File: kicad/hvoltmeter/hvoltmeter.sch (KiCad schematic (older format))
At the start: 34 parts, among them J1 USB_B_Micro-Connector, J2 SWC, J3 SWD, J4 Conn, J5 Conn, J6 Conn, SW1 SW_DPDT_x2, U1 LTC4054ES5-4.2, U2 AD8541, U3 MCP1700

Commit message: удалено:       STM32Cube/HV/.cproject 	удалено:       STM32Cube/HV/.mxproject 	удалено:       STM32Cube/HV/.project 	удалено:       STM32Cube/HV/.settings/language.settings.xml 	удалено:       STM32Cube/HV/.settings/stm32cubeide.project.prefs 	удалено:       STM32Cube/HV/Core/Inc/main.h 	удалено:       STM32Cube/HV/Core/Inc/stm32g0xx_hal_conf.h 	удалено:       STM32Cube/HV/Core/Inc/stm32g0xx_it.h 	удалено:       STM32Cube/HV/Core/Src/main.c 	удалено:       STM32Cube/HV/Core/Src/stm32g0xx_hal_msp.c 	удалено:       STM32Cube/HV/Core/Src/stm32g0xx_it.c 	удалено:       STM32Cube/HV/Core/Src/syscalls.c 	удалено:       STM32Cube/HV/Core/Src/sysmem.c 	удалено:       STM32Cube/HV/Core/Src/system_stm32g0xx.c 	удалено:       STM32Cube/HV/Core/Startup/startup_stm32g031f8px.s 	удалено:       STM32Cube/HV/Drivers/CMSIS/Device/ST/STM32G0xx/Include/stm32g031xx.h 	удалено:       STM32Cube/HV/Drivers/CMSIS/Device/ST/STM32G0xx/Include/stm32g0xx.h 	удалено:       STM32Cube/HV/Drivers/CMSIS/Device/ST/STM32G0xx/Include/system_stm32g0xx.h 	удалено:       STM32Cube/HV/Drivers/CMSIS/Include/cmsis_armcc.h 	удалено:       STM32Cube/HV/Drivers/CMSIS/Include/cmsis_armclang.h 	удалено:       STM32Cube/HV/Drivers/CMSIS/Include/cmsis_armclang_ltm.h 	удалено:       STM32Cube/HV/Drivers/CMSIS/Include/cmsis_compiler.h 	удалено:       STM32Cube/HV/Drivers/CMSIS/Include/cmsis_gcc.h 	удалено:       STM32Cube/HV/Drivers/CMSIS/Include/cmsis_iccarm.h 	удалено:       STM32Cube/HV/Drivers/CMSIS/Include/cmsis_version.h 	удалено:       STM32Cube/HV/Drivers/CMSIS/Include/core_armv81mml.h 	удалено:       STM32Cube/HV/Drivers/CMSIS/Include/core_armv8mbl.h 	удалено:       STM32Cube/HV/Drivers/CMSIS/Include/core_armv8mml.h 	удалено:       STM32Cube/HV/Drivers/CMSIS/Include/core_cm0.h 	удалено:       STM32Cube/HV/Drivers/CMSIS/Include/core_cm0plus.h 	удалено:       STM32Cube/HV/Drivers/CMSIS/Include/core_cm1.h 	удалено:       STM32Cube/HV/Drivers/CMSIS/Include/core_cm23.h 	удалено:       STM32Cube/HV/Drivers/CMSIS/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
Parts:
- D2: symbol My_Library:STM32G031F8-My_Library -> hvoltmeter-rescue:STM32G031F8-My_Library-My_Library
- D3: symbol My_Library:OLED049 -> hvoltmeter-rescue:OLED049-My_Library
- J1: symbol My_Library:USB_B_Micro-Connector -> hvoltmeter-rescue:USB_B_Micro-Connector-My_Library
- J2, J3, J4, J5, J6: symbol My_Library:Conn -> hvoltmeter-rescue:Conn-My_Library
- R6: value 10G -> 5G
- R8: value 4.7k -> 10k
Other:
- moved on the sheet: R8
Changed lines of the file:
@@
 $EndComp
 $Comp
-L My_Library:USB_B_Micro-Connector J1
+L hvoltmeter-rescue:USB_B_Micro-Connector-My_Library J1
 U 1 1 632D2EFA
 P 2650 3000
@@
 $EndComp
 $Comp
-L My_Library:STM32G031F8-My_Library D2
+L hvoltmeter-rescue:STM32G031F8-My_Library-My_Library D2
 U 1 1 632D3B69
 P 2900 4550
@@
 $EndComp
 $Comp
-L My_Library:Conn J4
+L hvoltmeter-rescue:Conn-My_Library J4
 U 1 1 632DFC6A
 P 4450 3200
@@
 Connection ~ 3900 3700
 $Comp
-L My_Library:Conn J5
+L hvoltmeter-rescue:Conn-My_Library J5
 U 1 1 632FDD5C
 P 4450 3600
@@
 U 1 1 63336864
 P 4750 4850
-F 0 "R6" H 4820 4896 50  0000 L CNN
-F 1 "10G" H 4820 4805 50  0000 L CNN
+F 0 "R6" H 4550 5100 50  0000 L CNN
+F 1 "5G" H 4550 5000 50  0000 L CNN
 F 2 "Resistor_SMD:R_2512_6332Metric" V 4680 4850 50  0001 C CNN
 F 3 "~" H 4750 4850 50  0001 C CNN
@@
 $EndComp
 $Comp
-L My_Library:Conn J6
+L hvoltmeter-rescue:Conn-My_Library J6
 U 1 1 6334DD34
 P 4750 4600
@@
 NoConn ~ 3350 4800
 $Comp
-L My_Library:Conn J3
+L hvoltmeter-rescue:Conn-My_Library J3
 U 1 1 633707DA
 P 3450 4300
@@
 Connection ~ 5600 3000
 $Comp
-L My_Library:Conn J2
+L hvoltmeter-rescue:Conn-My_Library J2
 U 1 1 6336FFB2
 P 3450 4200
@@
 $EndComp
 $Comp
-L My_Library:OLED049 D3
+L hvoltmeter-rescue:OLED049-My_Library D3
 U 1 1 6342BAD8
 P 5650 4300
@@
 L power:+2V8 #PWR016
 U 1 1 63592993
-P 5150 4300
-F 0 "#PWR016" H 5150 4150 50  0001 C CNN
-F 1 "+2V8" V 5165 4428 50  0000 L CNN
-F 2 "" H 5150 4300 50  0001 C CNN
-F 3 "" H 5150 4300 50  0001 C CNN
-	1    5150 4300
+P 5000 4300
+F 0 "#PWR016" H 5000 4150 50  0001 C CNN
+F 1 "+2V8" V 5015 4428 50  0000 L CNN
+F 2 "" H 5000 4300 50  0001 C CNN
+F 3 "" H 5000 4300 50  0001 C CNN
+	1    5000 4300
 	0    -1   -1   0
 $EndComp
@@
 L Device:R R8
 U 1 1 6359D97D
-P 5300 4700
-F 0 "R8" V 5300 4600 50  0000 L CNN
-F 1 "4.7k" V 5400 4450 50  0000 L CNN
-F 2 "Resistor_SMD:R_0402_1005Metric" V 5230 4700 50  0001 C CNN
-F 3 "~" H 5300 4700 50  0001 C CNN
-	1    5300 4700
-	0    1    1    0
-$EndComp
-Wire Wire Line
-	5450 4600 5150 4600
-Wire Wire Line
-	5150 4600 5150 4700
-Connection ~ 5150 4600
+P 5000 4450
+F 0 "R8" H 5100 4400 50  0000 L CNN
+F 1 "10k" H 5100 4500 50  0000 L CNN
+F 2 "Resistor_SMD:R_0402_1005Metric" V 4930 4450 50  0001 C CNN
+F 3 "~" H 5000 4450 50  0001 C CNN
+	1    5000 4450
+	-1   0    0    1
+$EndComp
 Connection ~ 4600 5500
 Wire Wire Line
@@
 	4500 5550 4500 5300
 Wire Wire Line
-	5450 4300 5150 4300
-Wire Wire Line
-	5150 4300 5150 4600
-Connection ~ 5150 4300
+	5450 4300 5250 4300
 Wire Wire Line
 	3100 3700 3500 3700
@@
 Wire Wire Line
 	4450 3100 4500 3100
+Wire Wire Line
+	5250 4300 5250 4600
+Wire Wire Line
+	5250 4600 5450 4600
+Connection ~ 5250 4300
+Wire Wire Line
+	5250 4300 5000 4300
+Connection ~ 5000 4300
+Wire Wire Line
+	5000 4600 5000 4700
+Wire Wire Line
+	5000 4700 5450 4700
 $EndSCHEMATC

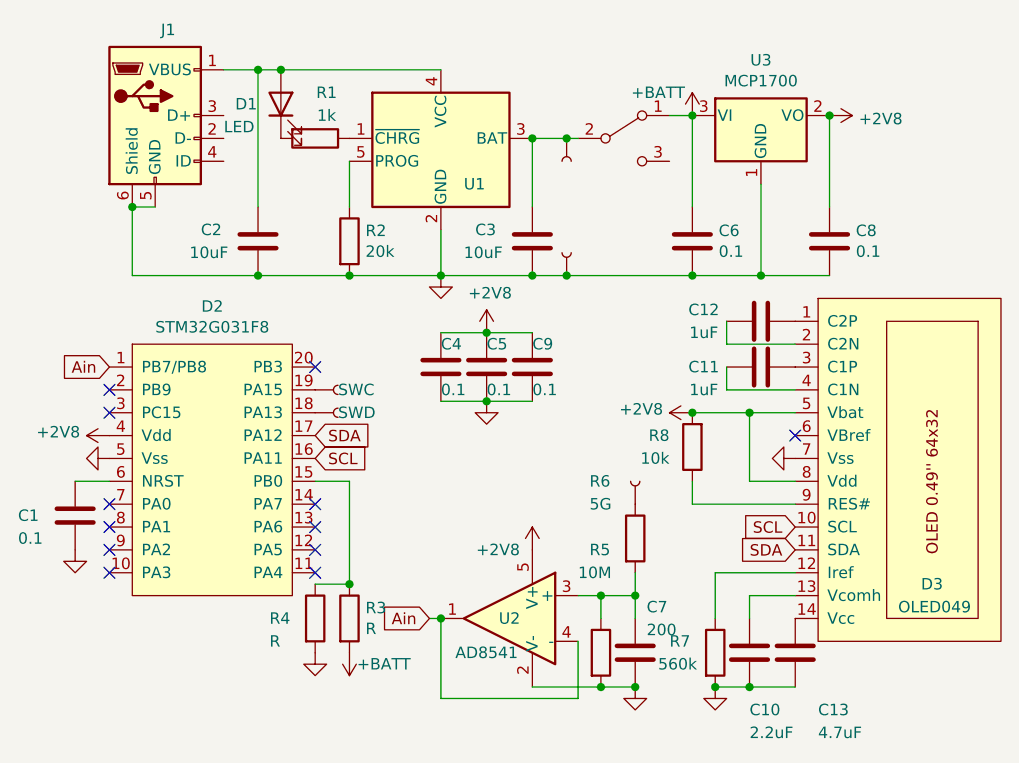
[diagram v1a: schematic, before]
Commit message: изменено:      kicad/hvoltmeter/hvoltmeter.kicad_pcb 	изменено:      kicad/hvoltmeter/hvoltmeter.kicad_pcb-bak 	изменено:      kicad/hvoltmeter/hvoltmeter.sch 	изменено:      kicad/hvoltmeter/hvoltmeter.sch-bak
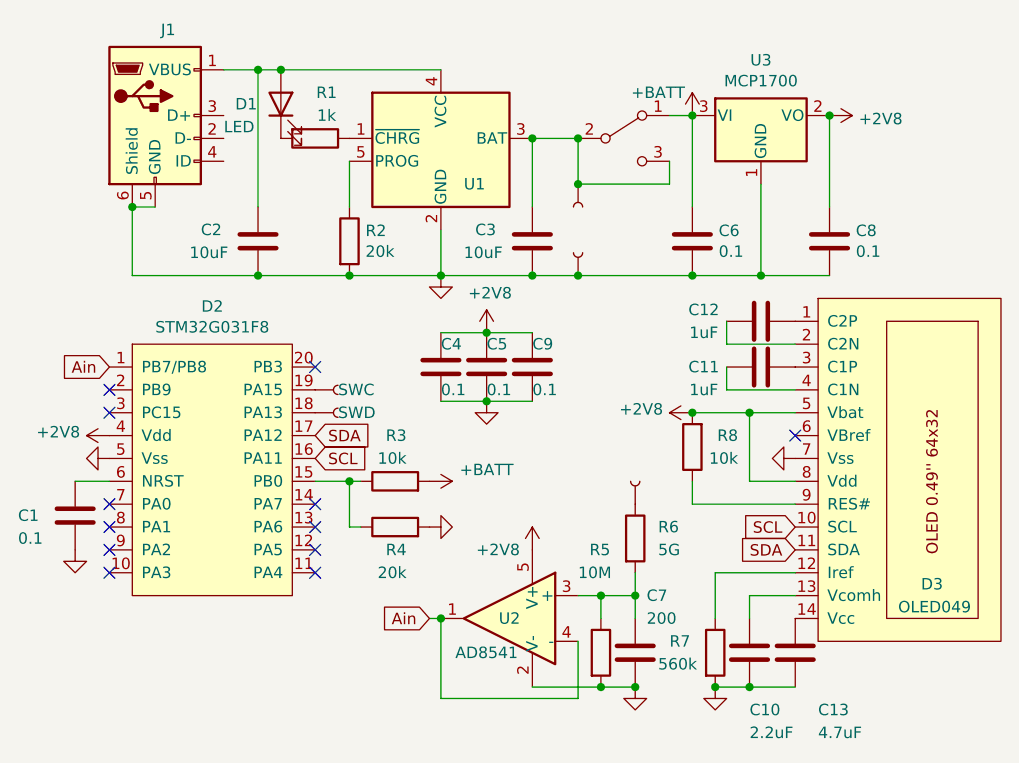
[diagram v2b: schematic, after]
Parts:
- R2: footprint Resistor_SMD:R_0603_1608Metric -> Resistor_SMD:R_0402_1005Metric
- R3: value R -> 10k; footprint Resistor_SMD:R_0603_1608Metric -> Resistor_SMD:R_0402_1005Metric
- R4: value R -> 20k; footprint Resistor_SMD:R_0603_1608Metric -> Resistor_SMD:R_0402_1005Metric
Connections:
- net at C3.1, J4.1, SW1.2 (B)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: now also SW1.3 (C)
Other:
- moved on the sheet: R3, R4
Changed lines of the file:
@@
 U 1 1 632CFD1F
 P 4750 5350
-F 0 "C7" H 4800 5550 50  0000 L CNN
-F 1 "200" H 4800 5450 50  0000 L CNN
+F 0 "C7" H 4800 5600 50  0000 L CNN
+F 1 "200" H 4800 5500 50  0000 L CNN
 F 2 "Capacitor_SMD:C_0603_1608Metric" H 4788 5200 50  0001 C CNN
 F 3 "~" H 4750 5350 50  0001 C CNN
@@
 L hvoltmeter-rescue:Conn-My_Library J4
 U 1 1 632DFC6A
-P 4450 3200
-F 0 "J4" V 4346 3248 50  0001 L CNN
-F 1 "Conn" V 4600 3200 50  0001 L CNN
-F 2 "My-library:SMD-CONN" H 4500 3050 50  0001 C CNN
-F 3 "~" H 4450 3200 50  0001 C CNN
-	1    4450 3200
+P 4500 3400
+F 0 "J4" V 4396 3448 50  0001 L CNN
+F 1 "Conn" V 4650 3400 50  0001 L CNN
+F 2 "My-library:SMD-CONN" H 4550 3250 50  0001 C CNN
+F 3 "~" H 4500 3400 50  0001 C CNN
+	1    4500 3400
 	0    1    1    0
 $EndComp
@@
 F 0 "R2" H 3570 3596 50  0000 L CNN
 F 1 "20k" H 3570 3505 50  0000 L CNN
-F 2 "Resistor_SMD:R_0603_1608Metric" V 3430 3550 50  0001 C CNN
+F 2 "Resistor_SMD:R_0402_1005Metric" V 3430 3550 50  0001 C CNN
 F 3 "~" H 3500 3550 50  0001 C CNN
 	1    3500 3550
@@
 L hvoltmeter-rescue:Conn-My_Library J5
 U 1 1 632FDD5C
-P 4450 3600
-F 0 "J5" V 4438 3552 50  0001 R CNN
-F 1 "Conn" V 4347 3552 50  0001 R CNN
-F 2 "My-library:SMD-CONN" H 4500 3450 50  0001 C CNN
-F 3 "~" H 4450 3600 50  0001 C CNN
-	1    4450 3600
+P 4500 3600
+F 0 "J5" V 4488 3552 50  0001 R CNN
+F 1 "Conn" V 4397 3552 50  0001 R CNN
+F 2 "My-library:SMD-CONN" H 4550 3450 50  0001 C CNN
+F 3 "~" H 4500 3600 50  0001 C CNN
+	1    4500 3600
 	0    -1   -1   0
 $EndComp
@@
 U 1 1 63336864
 P 4750 4850
-F 0 "R6" H 4550 5100 50  0000 L CNN
-F 1 "5G" H 4550 5000 50  0000 L CNN
+F 0 "R6" H 4850 4900 50  0000 L CNN
+F 1 "5G" H 4850 4800 50  0000 L CNN
 F 2 "Resistor_SMD:R_2512_6332Metric" V 4680 4850 50  0001 C CNN
 F 3 "~" H 4750 4850 50  0001 C CNN
@@
 L Device:R R3
 U 1 1 6335A741
-P 3500 5200
-F 0 "R3" H 3570 5246 50  0000 L CNN
-F 1 "R" H 3570 5155 50  0000 L CNN
-F 2 "Resistor_SMD:R_0603_1608Metric" V 3430 5200 50  0001 C CNN
-F 3 "~" H 3500 5200 50  0001 C CNN
-	1    3500 5200
-	1    0    0    -1
+P 3700 4600
+F 0 "R3" V 3900 4550 50  0000 L CNN
+F 1 "10k" V 3800 4550 50  0000 L CNN
+F 2 "Resistor_SMD:R_0402_1005Metric" V 3630 4600 50  0001 C CNN
+F 3 "~" H 3700 4600 50  0001 C CNN
+	1    3700 4600
+	0    -1   -1   0
 $EndComp
 $Comp
 L Device:R R4
 U 1 1 6335AF8C
-P 3350 5200
-F 0 "R4" H 3150 5200 50  0000 L CNN
-F 1 "R" H 3150 5100 50  0000 L CNN
-F 2 "Resistor_SMD:R_0603_1608Metric" V 3280 5200 50  0001 C CNN
-F 3 "~" H 3350 5200 50  0001 C CNN
-	1    3350 5200
-	1    0    0    -1
+P 3700 4800
+F 0 "R4" V 3600 4750 50  0000 L CNN
+F 1 "20k" V 3500 4750 50  0000 L CNN
+F 2 "Resistor_SMD:R_0402_1005Metric" V 3630 4800 50  0001 C CNN
+F 3 "~" H 3700 4800 50  0001 C CNN
+	1    3700 4800
+	0    -1   -1   0
 $EndComp
 $Comp
 L power:GND #PWR06
 U 1 1 6335B576
-P 3350 5350
-F 0 "#PWR06" H 3350 5100 50  0001 C CNN
-F 1 "GND" H 3355 5177 50  0001 C CNN
-F 2 "" H 3350 5350 50  0001 C CNN
-F 3 "" H 3350 5350 50  0001 C CNN
-	1    3350 5350
-	1    0    0    -1
+P 3850 4800
+F 0 "#PWR06" H 3850 4550 50  0001 C CNN
+F 1 "GND" H 3855 4627 50  0001 C CNN
+F 2 "" H 3850 4800 50  0001 C CNN
+F 3 "" H 3850 4800 50  0001 C CNN
+	1    3850 4800
+	0    -1   -1   0
 $EndComp
 $Comp
@@
 L power:+BATT #PWR05
 U 1 1 6335C7CF
-P 3500 5350
-F 0 "#PWR05" H 3500 5200 50  0001 C CNN
-F 1 "+BATT" H 3350 5400 50  0000 C CNN
-F 2 "" H 3500 5350 50  0001 C CNN
-F 3 "" H 3500 5350 50  0001 C CNN
-	1    3500 5350
-	-1   0    0    1
+P 3850 4600
+F 0 "#PWR05" H 3850 4450 50  0001 C CNN
+F 1 "+BATT" V 3800 4850 50  0000 C CNN
+F 2 "" H 3850 4600 50  0001 C CNN
+F 3 "" H 3850 4600 50  0001 C CNN
+	1    3850 4600
+	0    1    1    0
 $EndComp
 NoConn ~ 2450 4200
@@
 	3350 4600 3500 4600
 Wire Wire Line
-	3500 4600 3500 5050
-Wire Wire Line
-	3350 5050 3500 5050
-Connection ~ 3500 5050
+	3500 4600 3500 4800
 Text GLabel 2450 4100 0    50   Input ~ 0
 Ain
@@
 U 1 1 6359D97D
 P 5000 4450
-F 0 "R8" H 5100 4400 50  0000 L CNN
-F 1 "10k" H 5100 4500 50  0000 L CNN
+F 0 "R8" H 4800 4400 50  0000 L CNN
+F 1 "10k" H 4800 4500 50  0000 L CNN
 F 2 "Resistor_SMD:R_0402_1005Metric" V 4930 4450 50  0001 C CNN
 F 3 "~" H 5000 4450 50  0001 C CNN
@@
 Connection ~ 3100 2800
 Wire Wire Line
-	4300 3700 4450 3700
-Connection ~ 4450 3700
-Wire Wire Line
-	4450 3700 5000 3700
-Wire Wire Line
-	4300 3100 4450 3100
-Connection ~ 4450 3100
-Wire Wire Line
-	4450 3100 4500 3100
-Wire Wire Line
 	5250 4300 5250 4600
 Wire Wire Line
@@
 Wire Wire Line
 	5000 4700 5450 4700
+Wire Wire Line
+	3500 4600 3550 4600
+Connection ~ 3500 4600
+Wire Wire Line
+	3500 4800 3550 4800
+Wire Wire Line
+	4500 3100 4500 3300
+Wire Wire Line
+	4500 3300 4900 3300
+Wire Wire Line
+	4900 3300 4900 3200
+Connection ~ 4500 3100
+Connection ~ 4500 3300
+Connection ~ 4500 3700
+Wire Wire Line
+	4500 3700 5000 3700
+Wire Wire Line
+	4300 3100 4500 3100
+Wire Wire Line
+	4300 3700 4500 3700
 $EndSCHEMATC

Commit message: изменено:      kicad/hvoltmeter/hvoltmeter.kicad_pcb 	изменено:      kicad/hvoltmeter/hvoltmeter.kicad_pcb-bak 	изменено:      kicad/hvoltmeter/hvoltmeter.sch 	изменено:      kicad/hvoltmeter/hvoltmeter.sch-bak
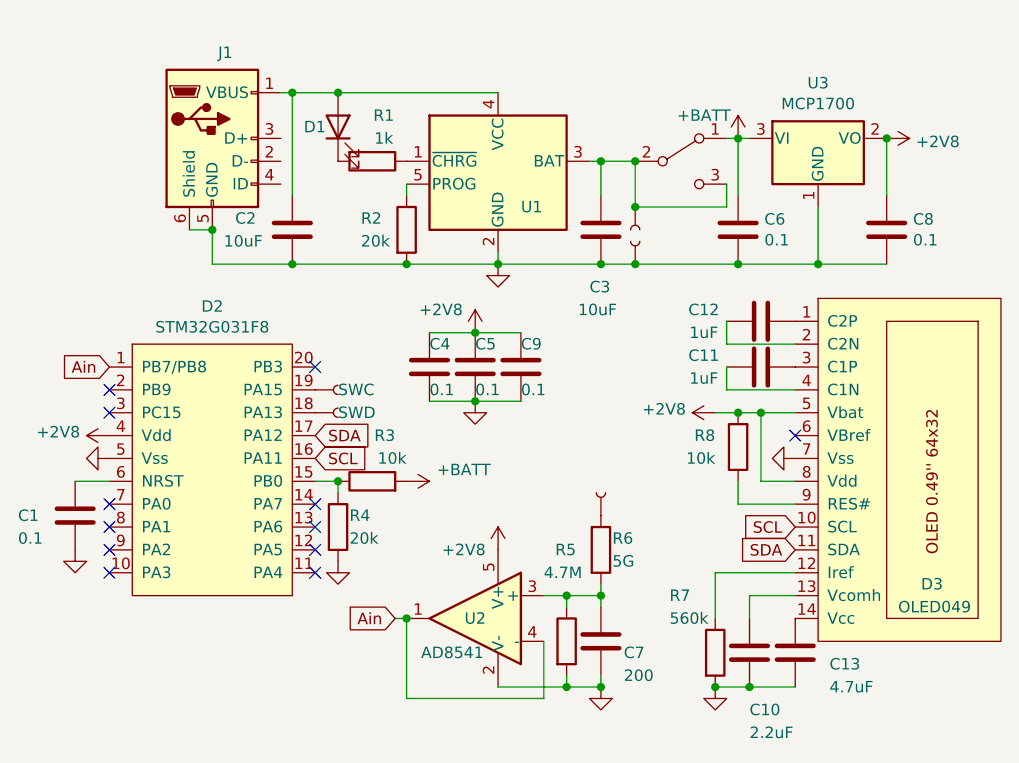
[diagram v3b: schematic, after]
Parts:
- R5: value 10M -> 4.7M
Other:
- moved on the sheet: C2, C3, C4, C5, C6, C7, C8, C9, D1, J1, R1, R2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

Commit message: изменено:      kicad/hvoltmeter/hvoltmeter.kicad_pcb 	изменено:      kicad/hvoltmeter/hvoltmeter.kicad_pcb-bak 	изменено:      kicad/hvoltmeter/hvoltmeter.sch 	изменено:      kicad/hvoltmeter/hvoltmeter.sch-bak
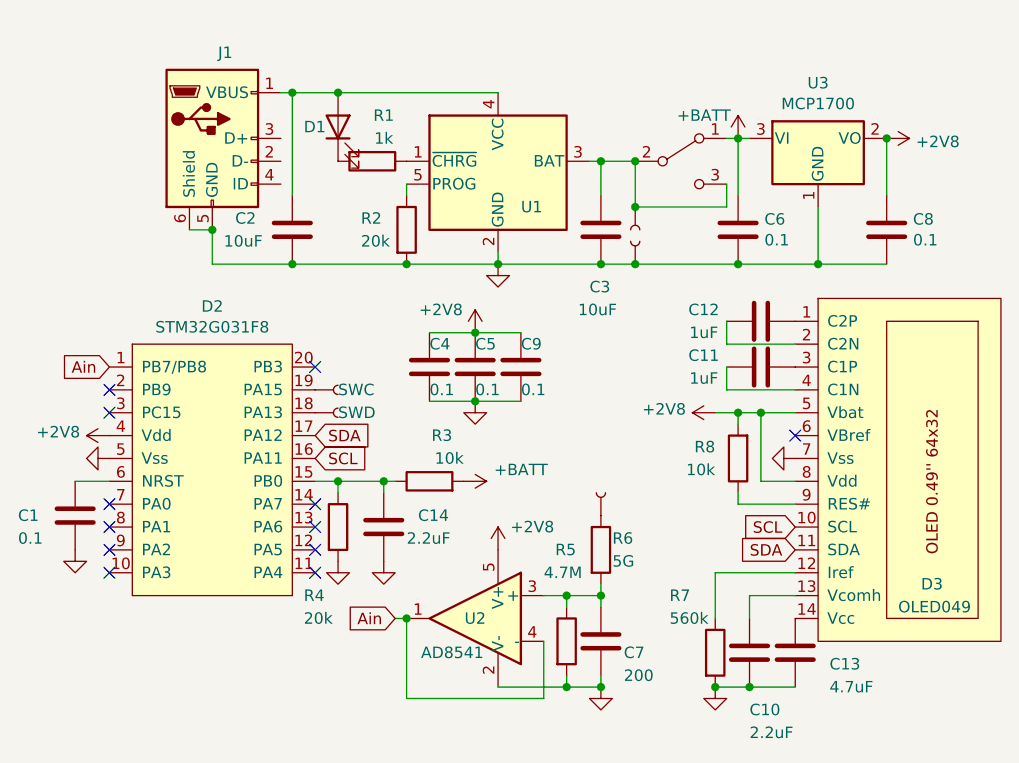
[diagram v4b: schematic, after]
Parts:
- added C14: 2.2uF, Capacitor_SMD:C_0402_1005Metric, symbol Device:C
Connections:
- net GND: now also C14.1
- net at D2.15 (PB0), R3.1, R4.1: now also C14.2
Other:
- moved on the sheet: R3, R8
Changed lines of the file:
@@
 P 4150 4900
 F 0 "#PWR07" H 4150 4750 50  0001 C CNN
-F 1 "+2V8" H 4000 4900 50  0000 C CNN
+F 1 "+2V8" H 4300 5000 50  0000 C CNN
 F 2 "" H 4150 4900 50  0001 C CNN
 F 3 "" H 4150 4900 50  0001 C CNN
@@
 L Device:R R3
 U 1 1 6335A741
-P 3600 4600
-F 0 "R3" V 3800 4500 50  0000 L CNN
-F 1 "10k" V 3700 4450 50  0000 L CNN
-F 2 "Resistor_SMD:R_0402_1005Metric" V 3530 4600 50  0001 C CNN
-F 3 "~" H 3600 4600 50  0001 C CNN
-	1    3600 4600
+P 3850 4600
+F 0 "R3" V 4050 4500 50  0000 L CNN
+F 1 "10k" V 3950 4450 50  0000 L CNN
+F 2 "Resistor_SMD:R_0402_1005Metric" V 3780 4600 50  0001 C CNN
+F 3 "~" H 3850 4600 50  0001 C CNN
+	1    3850 4600
 	0    -1   -1   0
 $EndComp
@@
 U 1 1 6335AF8C
 P 3450 4800
-F 0 "R4" H 3500 4850 50  0000 L CNN
-F 1 "20k" H 3500 4750 50  0000 L CNN
+F 0 "R4" H 3300 4500 50  0000 L CNN
+F 1 "20k" H 3300 4400 50  0000 L CNN
 F 2 "Resistor_SMD:R_0402_1005Metric" V 3380 4800 50  0001 C CNN
 F 3 "~" H 3450 4800 50  0001 C CNN
@@
 L power:+BATT #PWR05
 U 1 1 6335C7CF
-P 3750 4600
-F 0 "#PWR05" H 3750 4450 50  0001 C CNN
-F 1 "+BATT" V 3700 4850 50  0000 C CNN
-F 2 "" H 3750 4600 50  0001 C CNN
-F 3 "" H 3750 4600 50  0001 C CNN
-	1    3750 4600
+P 4000 4600
+F 0 "#PWR05" H 4000 4450 50  0001 C CNN
+F 1 "+BATT" V 3950 4850 50  0000 C CNN
+F 2 "" H 4000 4600 50  0001 C CNN
+F 3 "" H 4000 4600 50  0001 C CNN
+	1    4000 4600
 	0    1    1    0
 $EndComp
@@
 L Device:R R8
 U 1 1 6359D97D
-P 5200 4450
-F 0 "R8" H 5300 4400 50  0000 L CNN
-F 1 "10k" H 5300 4500 50  0000 L CNN
-F 2 "Resistor_SMD:R_0402_1005Metric" V 5130 4450 50  0001 C CNN
-F 3 "~" H 5200 4450 50  0001 C CNN
-	1    5200 4450
+P 5200 4500
+F 0 "R8" H 5300 4450 50  0000 L CNN
+F 1 "10k" H 5300 4550 50  0000 L CNN
+F 2 "Resistor_SMD:R_0402_1005Metric" V 5130 4500 50  0001 C CNN
+F 3 "~" H 5200 4500 50  0001 C CNN
+	1    5200 4500
 	-1   0    0    1
 $EndComp
@@
 Wire Wire Line
 	3450 4650 3450 4600
-Connection ~ 3450 4600
 Wire Wire Line
 	4350 5100 4450 5100
@@
 	5200 4300 5300 4300
 Wire Wire Line
-	5200 4600 5200 4700
-Wire Wire Line
 	5100 4300 5200 4300
 Wire Wire Line
@@
 	4600 5050 4600 5100
 Connection ~ 4600 5100
+$Comp
+L Device:C C14
+U 1 1 633643EB
+P 3650 4800
+F 0 "C14" H 3500 4750 50  0000 R CNN
+F 1 "2.2uF" H 3550 4850 50  0000 R CNN
+F 2 "Capacitor_SMD:C_0402_1005Metric" H 3688 4650 50  0001 C CNN
+F 3 "~" H 3650 4800 50  0001 C CNN
+	1    3650 4800
+	-1   0    0    1
+$EndComp
+$Comp
+L power:GND #PWR015
+U 1 1 63364C26
+P 3650 4950
+F 0 "#PWR015" H 3650 4700 50  0001 C CNN
+F 1 "GND" H 3655 4777 50  0001 C CNN
+F 2 "" H 3650 4950 50  0001 C CNN
+F 3 "" H 3650 4950 50  0001 C CNN
+	1    3650 4950
+	1    0    0    -1
+$EndComp
+Wire Wire Line
+	3450 4600 3650 4600
+Connection ~ 3450 4600
+Wire Wire Line
+	3650 4650 3650 4600
+Connection ~ 3650 4600
+Wire Wire Line
+	3650 4600 3700 4600
+Wire Wire Line
+	5200 4300 5200 4350
+Wire Wire Line
+	5200 4650 5200 4700
 $EndSCHEMATC
